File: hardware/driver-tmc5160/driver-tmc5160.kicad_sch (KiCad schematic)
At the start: 41 parts, among them J1 Micro-Fit, U1 TMC5160A-TA

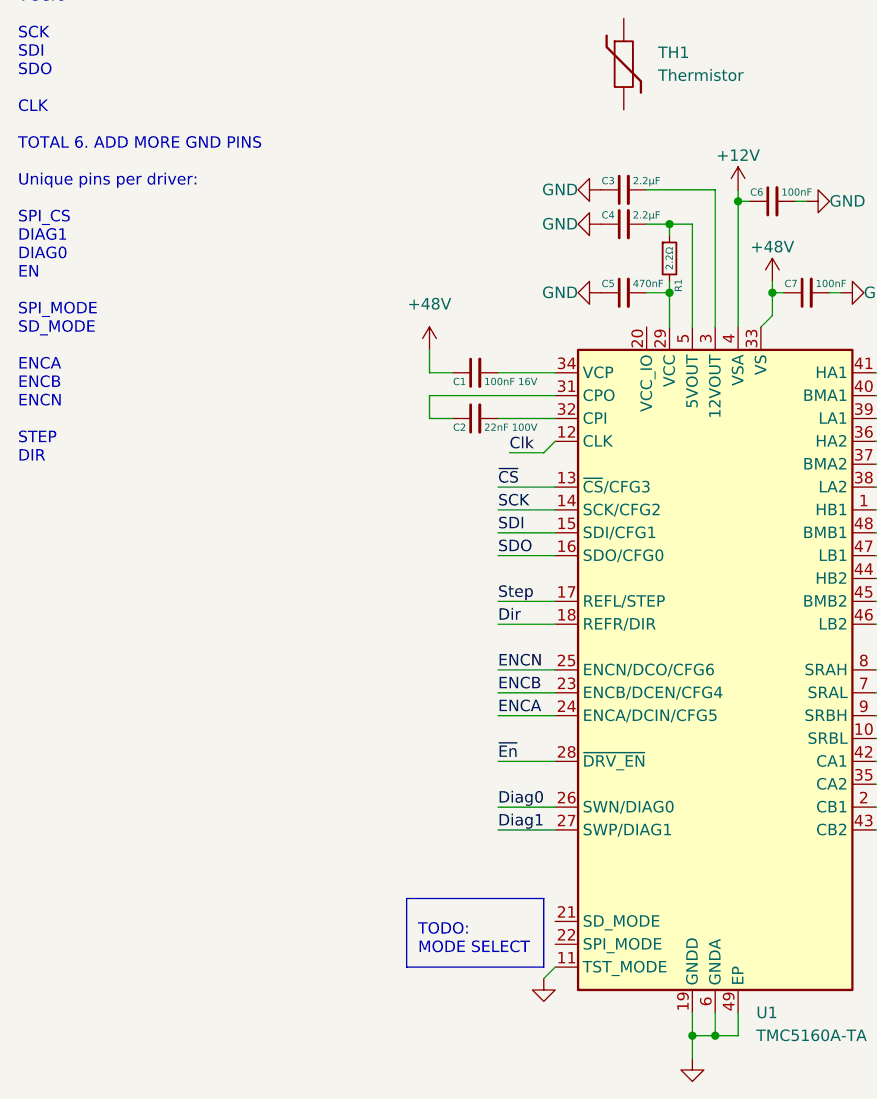
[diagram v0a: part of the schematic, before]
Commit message: added preliminary LGA layout for motor expansion module
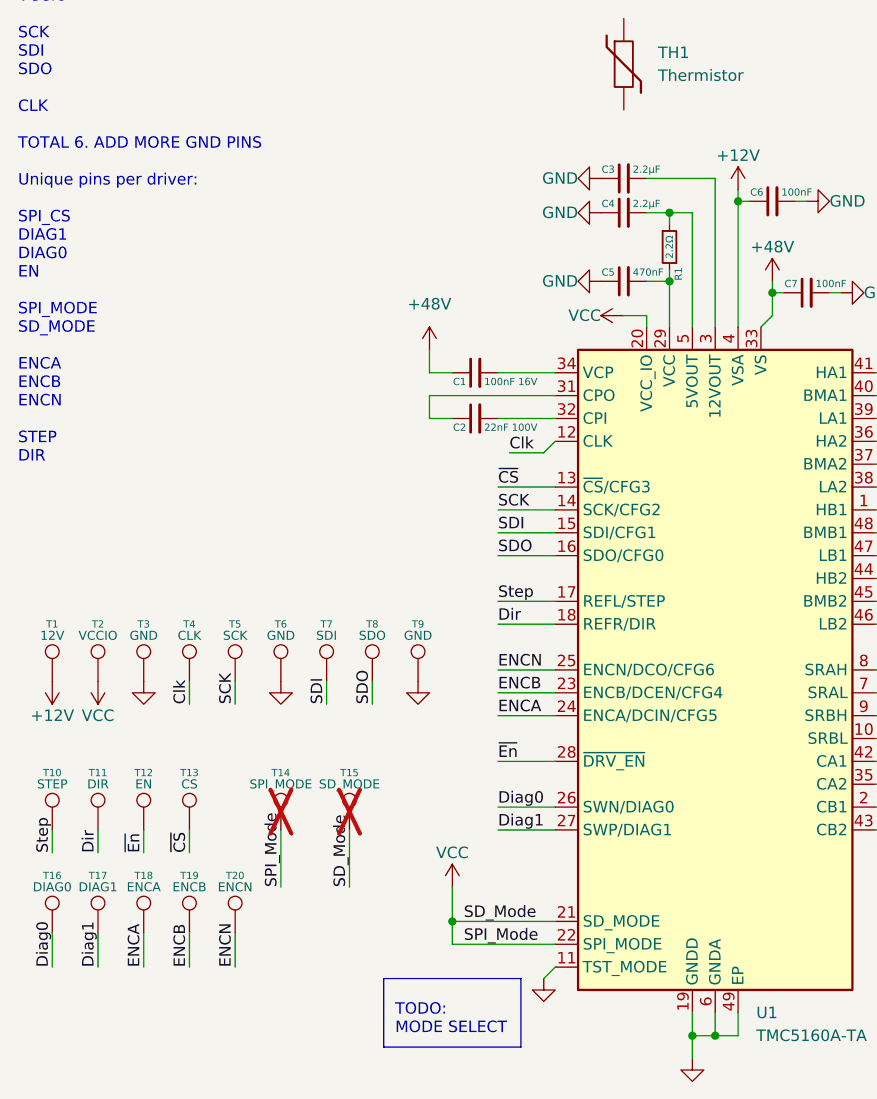
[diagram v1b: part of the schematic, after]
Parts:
- added T1: 12V, corevus:LGA_Land, symbol Connector:TestPoint
- added T10: STEP, corevus:LGA_Land, symbol Connector:TestPoint
- added T11: DIR, corevus:LGA_Land, symbol Connector:TestPoint
- added T12: EN, corevus:LGA_Land, symbol Connector:TestPoint
- added T13: CS, corevus:LGA_Land, symbol Connector:TestPoint
- added T14: SPI_MODE, corevus:LGA_Land, symbol Connector:TestPoint
- added T15: SD_MODE, corevus:LGA_Land, symbol Connector:TestPoint
- added T16: DIAG0, corevus:LGA_Land, symbol Connector:TestPoint
- added T17: DIAG1, corevus:LGA_Land, symbol Connector:TestPoint
- added T18: ENCA, corevus:LGA_Land, symbol Connector:TestPoint
- added T19: ENCB, corevus:LGA_Land, symbol Connector:TestPoint
- added T2: VCCIO, corevus:LGA_Land, symbol Connector:TestPoint
- added T20: ENCN, corevus:LGA_Land, symbol Connector:TestPoint
- added T3, T6, T9: GND, corevus:LGA_Land, symbol Connector:TestPoint
- added T4: CLK, corevus:LGA_Land, symbol Connector:TestPoint
- added T5: SCK, corevus:LGA_Land, symbol Connector:TestPoint
- added T7: SDI, corevus:LGA_Land, symbol Connector:TestPoint
- added T8: SDO, corevus:LGA_Land, symbol Connector:TestPoint
- H1, H2: footprint tmc5160-driver:edge_mounting_hole -> corevus:MountingHole_M3_Driver
- J1: footprint tmc5160-driver:XKB_X3025WRS-04 -> corevus:XKB_X3025WRS-04
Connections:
- net +12V: now also T1.1
- net Clk: now also T4.1
- net Diag0: now also T16.1
- net Diag1: now also T17.1
- net Dir: now also T11.1
- net ENCA: now also T18.1
- net ENCB: now also T19.1
- net ENCN: now also T20.1
- net GND: now also T3.1, T6.1, T9.1
- net SCK: now also T5.1
- net SDI: now also T7.1
- net SDO: now also T8.1
- net Step: now also T10.1
- net ~{CS}: now also T13.1
- net ~{En}: now also T12.1
- net VCC: now reaches U1.20 (VCC_IO)
- net VCC: now also U1.21 (SD_MODE), U1.22 (SPI_MODE), T14.1, T15.1, T2.1
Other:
- moved on the sheet: C3, C4, C5, R1

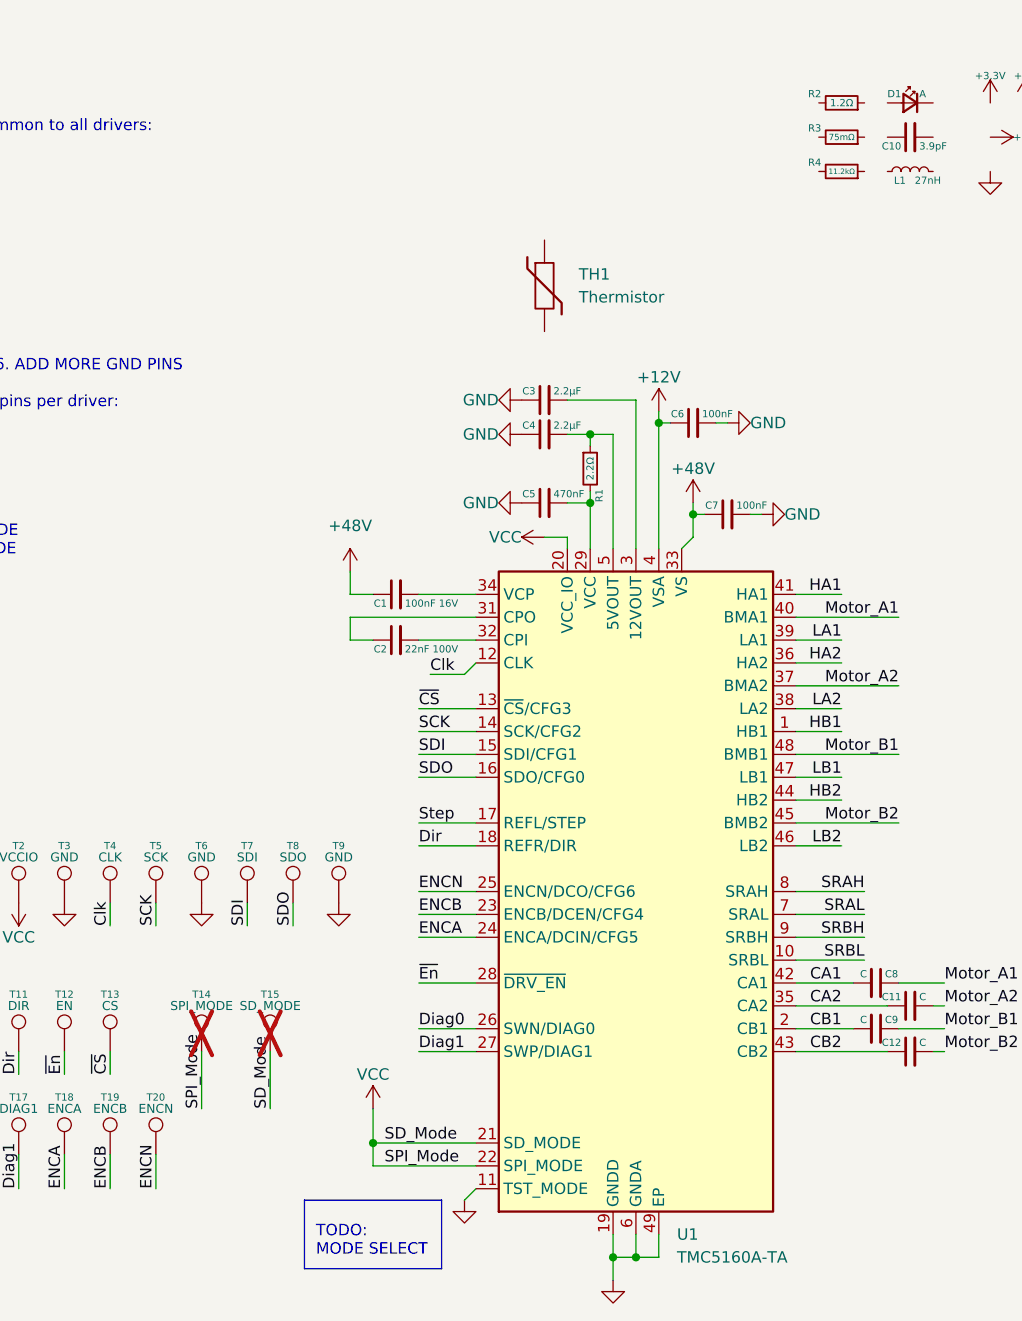
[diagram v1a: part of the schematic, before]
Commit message: further work on motor drivers and connector layout, additional symbols/footprints/models
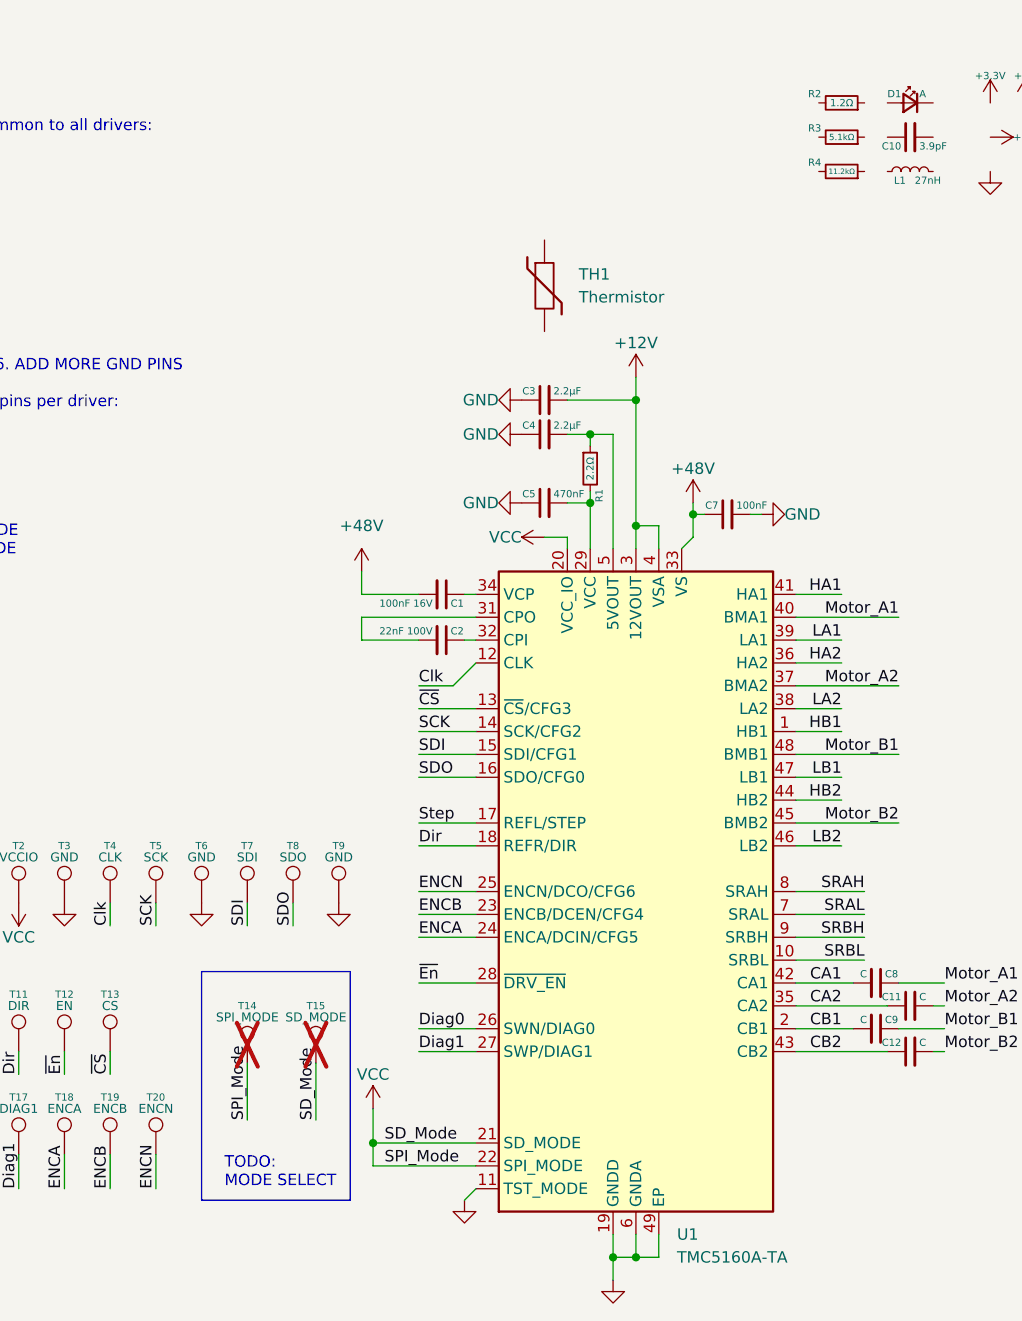
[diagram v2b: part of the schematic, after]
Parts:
- removed C6: 100nF, AlphaLib:0402C, symbol Device:C_Small
- R3: value 75mΩ -> 5.1kΩ
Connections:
- net +12V: now also C3.2, U1.3 (12VOUT)
- net +48V: now also C1.2; no longer C1.1
- net at U1.34 (VCP): now also C1.1; no longer C1.2
- net at U1.31 (CPO): now also C2.2; no longer C2.1
- net at U1.32 (CPI): now also C2.1; no longer C2.2
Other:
- moved on the sheet: C1, C2, T14, T15

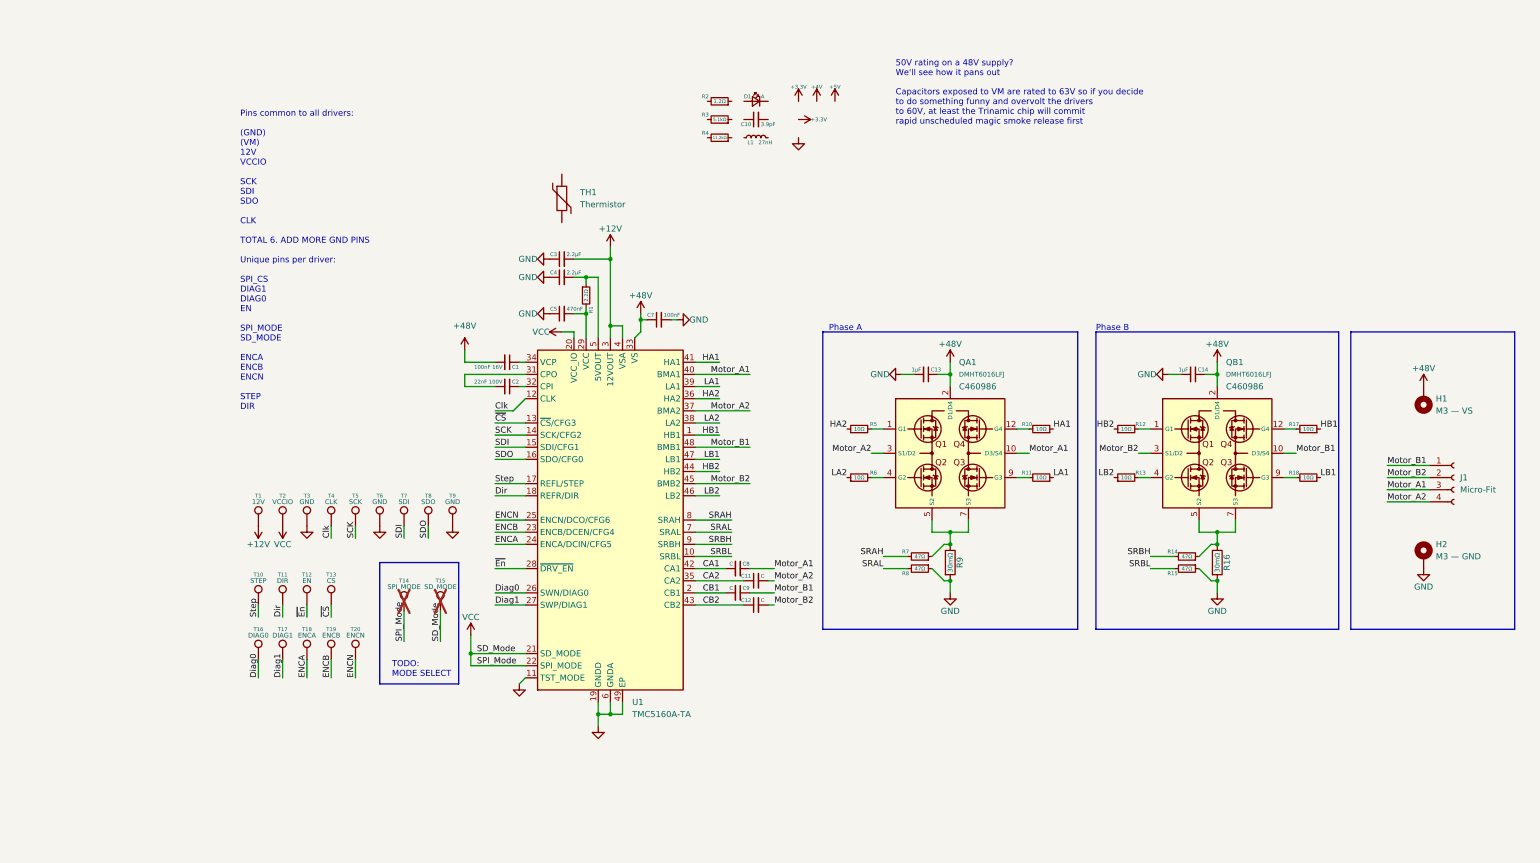
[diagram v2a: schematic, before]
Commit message: redid mainboard, added probe wiring, replacing ncp chip with LM5160 for now
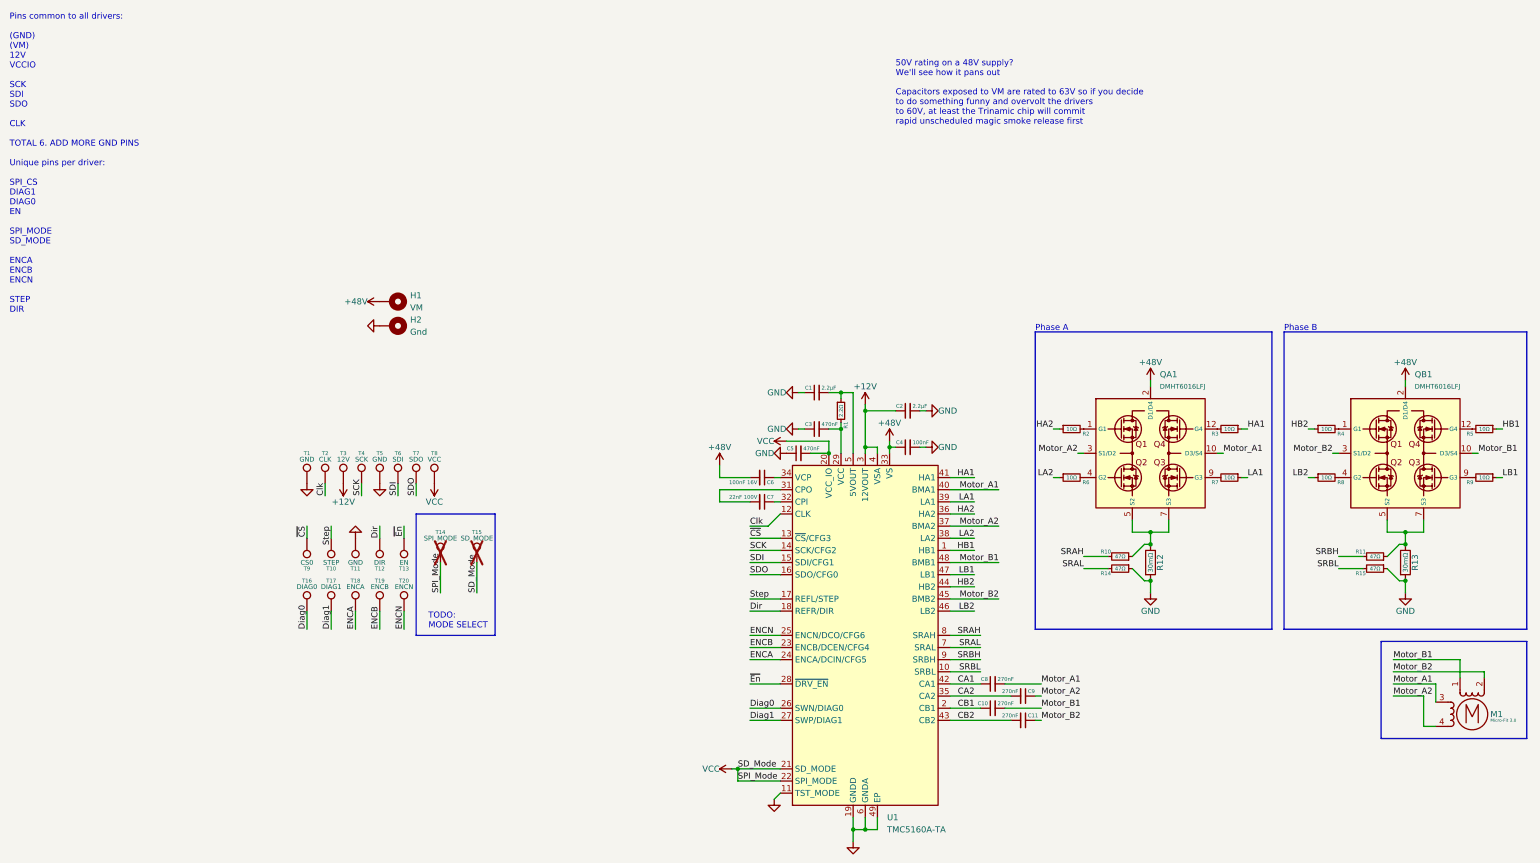
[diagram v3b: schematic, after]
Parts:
- removed C12: C, AlphaLib:0402C, symbol Device:C_Small
- removed C13, C14: 1μF, Capacitor_SMD:C_0805_2012Metric, symbol Device:C_Small
- removed D1: A, symbol Device:LED_Small
- removed J1: Micro-Fit, corevus:XKB_X3025WRS-04, symbol Connector:Conn_01x04_Female
- removed L1: 27nH, symbol Device:L_Small
- removed R12, R13, R17, R18: 10Ω, AlphaLib:0402R, symbol Device:R_Small
- removed R16, R9: 30mΩ, Resistor_SMD:R_0805_2012Metric, symbol Device:R
- removed T13: CS, corevus:LGA_Land, symbol Connector:TestPoint
- removed TH1: Thermistor, AlphaLib:0603R, symbol Device:Thermistor
- added C6: 100nF 16V, AlphaLib:0402C, symbol Device:C_Small
- added M1: Micro-Fit 3.0, corevus:XKB_X3025WRS-04D, symbol Motor:Stepper_Motor_bipolar
- added R12, R13: 30mΩ, Resistor_SMD:R_1206_3216Metric, symbol Device:R
- added R9: 10Ω, AlphaLib:0402R, symbol Device:R_Small
- added T5: GND, corevus:LGA_Land, symbol Connector:TestPoint
- C1: value 100nF 16V -> 2.2μF
- C10: value 3.9pF -> 270nF; footprint (none) -> AlphaLib:0402C
- C11, C8, C9: value C -> 270nF
- C2: value 22nF 100V -> 2.2μF
- C3: value 2.2μF -> 470nF
- C4: value 2.2μF -> 100nF
- C7: value 100nF -> 22nF 100V
- H1: value M3 — VS -> VM
- H2: value M3 — GND -> Gnd
- R1: footprint (none) -> AlphaLib:0402R
- R10, R11: value 10Ω -> 47Ω
- R2: value 1.2Ω -> 10Ω; footprint (none) -> AlphaLib:0402R
- R3: value 5.1kΩ -> 10Ω; footprint (none) -> AlphaLib:0402R
- R4: value 11.2kΩ -> 10Ω; footprint (none) -> AlphaLib:0402R
- R7, R8: value 47Ω -> 10Ω
- T8: renamed from T2; value VCCIO -> VCC
- T9: value GND -> CS0
- renumbered T3 to T1, T6 to T11, T11 to T12, T12 to T13, T4 to T2, T1 to T3, T5 to T4, T7 to T6, T8 to T7
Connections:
- net +12V: now also C2.1; no longer C3.2
- net +48V: now also C4.1, C6.2; no longer C1.2, C7.1
- net CA1: now also C8.1; no longer C8.2
- net CA2: now also C9.2; no longer C11.1
- net CB1: now also C10.1; no longer C9.2
- net CB2: now also C11.2
- net GND: now also C1.1, C2.2, C4.2, R14.1, R12.2, R13.2, T5.1; no longer C4.1, C7.2, R8.1, T9.1
- net HA1: now also R3.1; no longer R10.1
- net HA2: now also R2.1; no longer R5.1
- net HB1: now also R5.1
- net HB2: now also R4.1
- net LA1: now also R7.1; no longer R11.1
- net LB1: now also R9.1
- net LB2: now also R8.1
- net Motor_A1: now also C8.2, M1.3; no longer C8.1
- net Motor_A2: now also C9.1, M1.4; no longer C11.2
- net Motor_B1: now also C10.2, M1.1; no longer C9.1
- net Motor_B2: now also C11.1, M1.2 (-)
- net SRAH: now also R10.2; no longer R7.2
- net SRAL: now also R14.2; no longer R8.2
- net SRBH: now also R11.2; no longer R14.2
- net VCC: now also C5.2
- net ~{CS}: now also T9.1
- net at QB1.9 (G3): now also R9.2
- net at R1.1, U1.5 (5VOUT): now also C1.2; no longer C4.2
- net at R1.2, U1.29 (VCC): now also C3.2; no longer C5.2
- net at QA1.9 (G3): now also R7.2; no longer R11.2
- net at U1.34 (VCP): now also C6.1; no longer C1.1
- net at R4.2: now also QB1.1 (G1)
- net at QB1.12 (G4): now also R5.2
- net at U1.31 (CPO): now also C7.2; no longer C2.2
- net at U1.32 (CPI): now also C7.1; no longer C2.1
- net at QB1.5 (S2), QB1.6 (S2), QB1.7 (S3)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: now also R11.1, R13.1; no longer R14.1
- net at R3.2: now also QA1.12 (G4)
- net at QA1.5 (S2), QA1.6 (S2), QA1.7 (S3)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: now also R10.1, R12.1; no longer R7.1
- net at QA1.1 (G1): now also R2.2; no longer R5.2
- net at QB1.4 (G2): now also R8.2
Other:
- moved on the sheet: T1, T10, T11, T12, T13, T14, T15, T16, T17, T18, T19, T2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

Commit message: nearing first prototype woot! copyediting over entire board, fixed some mistakes
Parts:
- added C12: 100nF 60V/2, AlphaLib:0402C, symbol Device:C_Small
- added C13: 47nF 100V, AlphaLib:0402C, symbol Device:C_Small
- C4: value 100nF -> 100nF 60V/2
- C7: value 22nF 100V -> 47nF 100V/2
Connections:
- net GND: now also C12.2; no longer C4.2
- net at U1.31 (CPO): now also C13.2; no longer C7.2
- new net: C12.1, C4.2
- new net: C13.1, C7.2

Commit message: test new gitignore with completed mainboard
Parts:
- C1, C2: value 2.2μF -> 1μF
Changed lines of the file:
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@@
       (effects (font (size 0.8 0.8)) (justify left))
     )
-    (property "Value" "2.2μF" (at 154.67 94.25 90)
+    (property "Value" "1μF" (at 154.67 94.25 90)
       (effects (font (size 0.8 0.8)) (justify right))
     )
@@
       (effects (font (size 0.8 0.8)) (justify left))
     )
-    (property "Value" "2.2μF" (at 135.62 90.44 90)
+    (property "Value" "1μF" (at 135.62 90.44 90)
       (effects (font (size 0.8 0.8)) (justify right))
     )
